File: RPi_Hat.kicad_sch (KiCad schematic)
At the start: 34 parts, among them IC1 0.96_I2C_OLED, IC2 0.96_I2C_OLED, J1 RPi_GPIO, J2 TCBM, J3 Conn_01x05, J4 Mini-DIN-7, Q1 NPN: 2n3904, Q2 NPN: 2n3904, Q3 NPN: 2n3904, Q4 NPN: 2n3904, SW1 Select, SW2 Up, SW3 Down, SW4 Exit, SW5 Add Disk

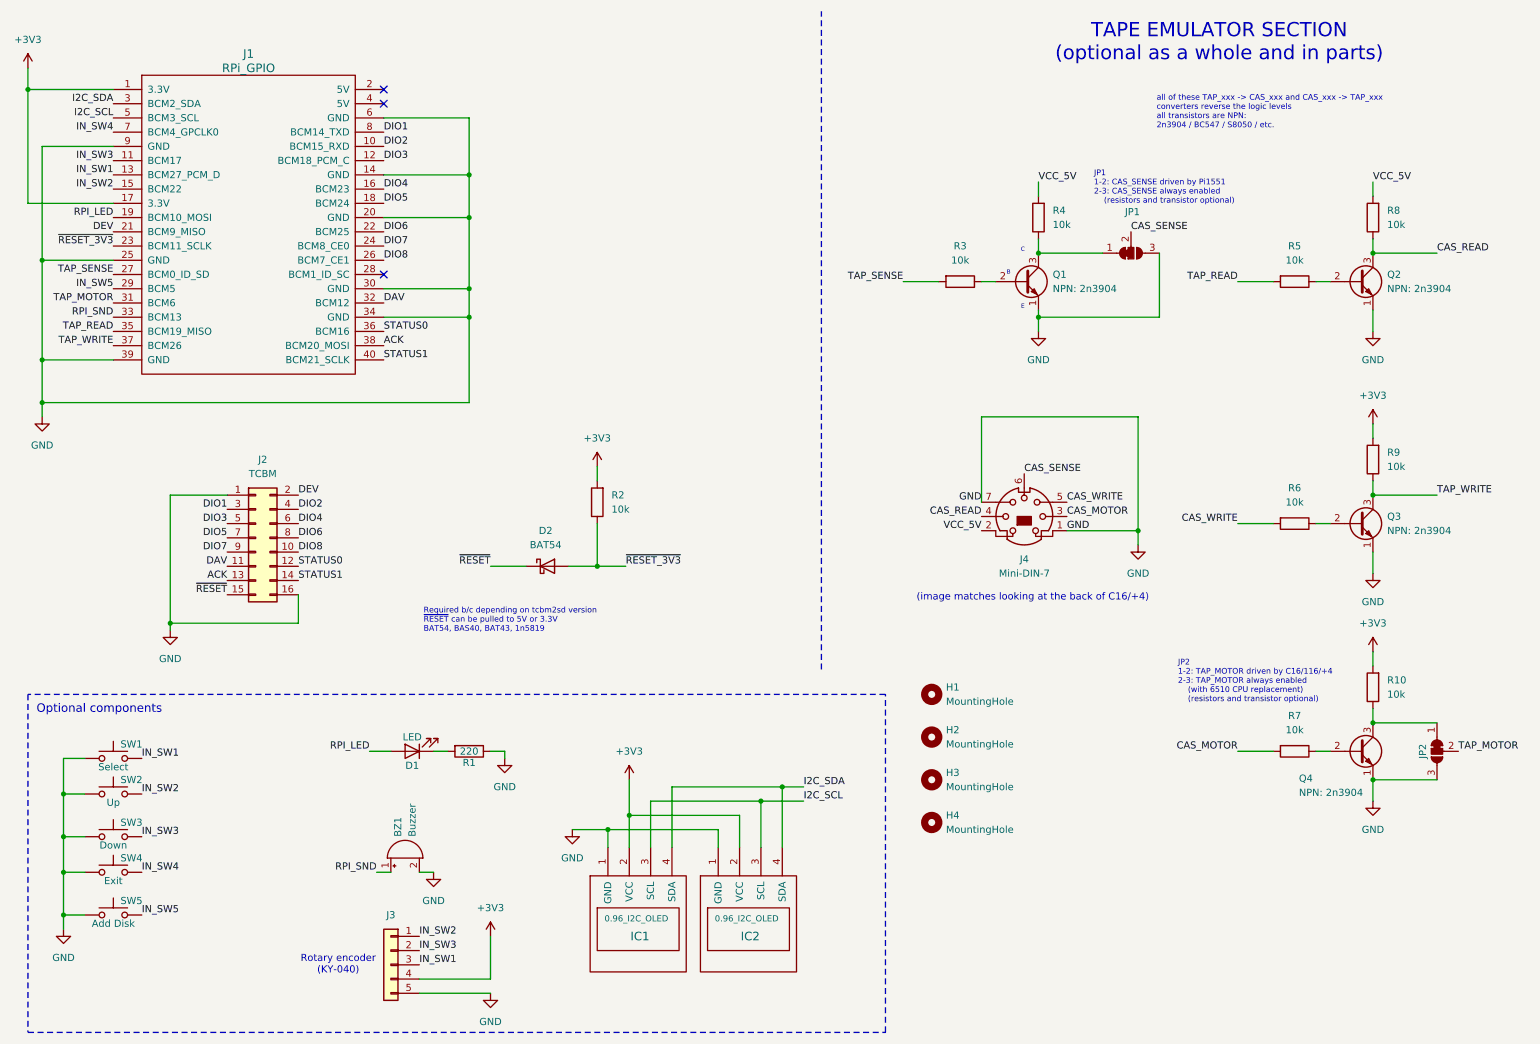
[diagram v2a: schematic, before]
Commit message: SMD rework and updates
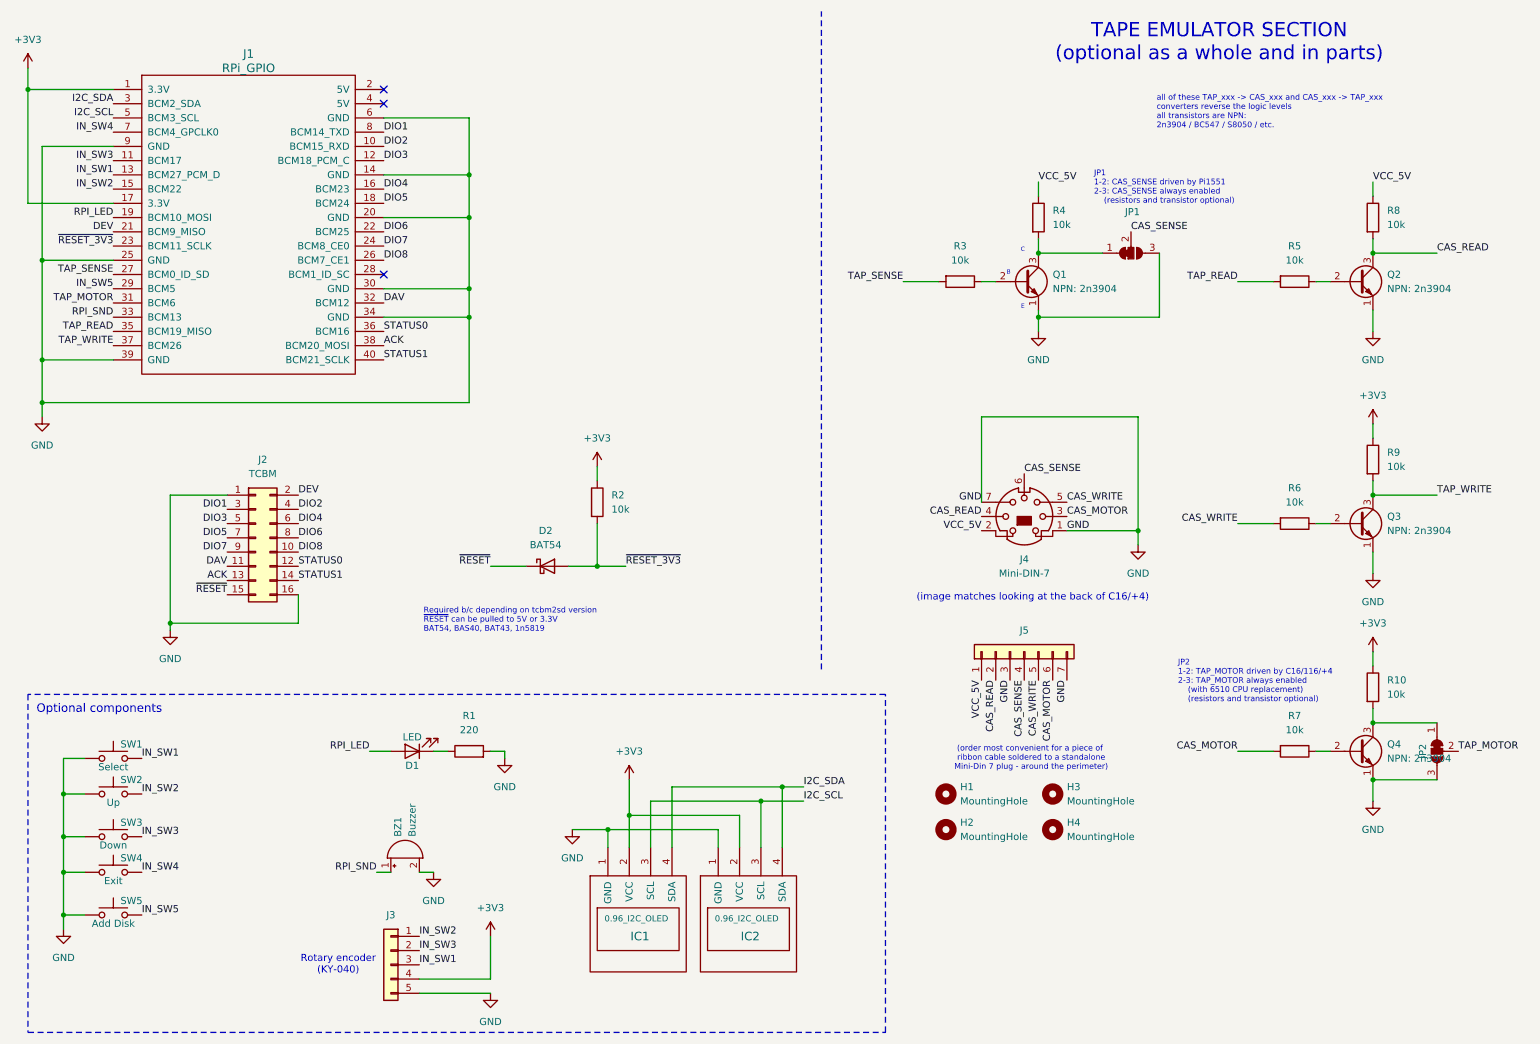
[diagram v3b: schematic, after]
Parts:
- added J5: Conn_01x07, Connector_PinHeader_2.54mm:PinHeader_1x07_P2.54mm_Horizontal, symbol Connector_Generic:Conn_01x07
- D1: footprint LED_THT:LED_D5.0mm -> LED_THT:LED_D3.0mm
- D2: footprint Diode_THT:D_A-405_P7.62mm_Horizontal -> Diode_SMD:D_SOD-123; JLCPCB Part # (none) -> C7502705; JLCPCB URL (none) -> https://jlcpcb.com/partdetail/hongjiacheng-BAT54W/C7502705; MFR.Part # (none) -> BAT54W
- J4: footprint Connector_PinHeader_2.54mm:PinHeader_1x07_P2.54mm_Vertical -> Conn_DIN_round:Mini_DIN_round_7_canned
- Q1, Q2, Q3, Q4: footprint Package_TO_SOT_THT:TO-92_Inline -> Package_TO_SOT_SMD:SOT-23_Handsoldering; JLCPCB Part # (none) -> C18536; JLCPCB URL (none) -> https://jlcpcb.com/partdetail/KECSemicon-2N3904S_RTKPS/C185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; MFR.Part # (none) -> 2N3904S-RTK/PS
- R1: footprint Resistor_THT:R_Axial_DIN0207_L6.3mm_D2.5mm_P10.16mm_Horizontal -> Resistor_SMD:R_0805_2012Metric_Pad1.20x1.40mm_HandSolder; JLCPCB Part # (none) -> C17557; JLCPCB URL (none) -> https://jlcpcb.com/partdetail/18245-0805W8F2200T5E/C17557; MFR.Part # (none) -> 0805W8F2200T5E
- R10, R2, R3, R4, R5, R6, R7, R8, R9: footprint Resistor_THT:R_Axial_DIN0207_L6.3mm_D2.5mm_P10.16mm_Horizontal -> Resistor_SMD:R_0805_2012Metric_Pad1.20x1.40mm_HandSolder; JLCPCB Part # (none) -> C22356686; JLCPCB URL (none) -> https://jlcpcb.com/partdetail/23790130-RCA0510KFLF/C22356686; MFR.Part # (none) -> RCA0510KFLF
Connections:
- net +3V3: now also R10.1, R2.1, R9.1; no longer R10.2, R2.2, R9.2
- net CAS_MOTOR: now also J5.6 (Pin_6)
- net CAS_READ: now also R8.2, J5.2 (Pin_2); no longer R8.1
- net CAS_SENSE: now also J5.4 (Pin_4)
- net CAS_WRITE: now also J5.5 (Pin_5)
- net GND: now also R1.2, J5.3 (Pin_3), J5.7 (Pin_7); no longer R1.1
- net TAP_WRITE: now also R9.2; no longer R9.1
- net VCC_5V: now also R4.1, R8.1, J5.1 (Pin_1); no longer R4.2, R8.2
- net ~{RESET_3V3}: now also R2.2; no longer R2.1
- net at D1.1 (K): now also R1.1; no longer R1.2
- net at JP1.1 (A), Q1.3 (C): now also R4.2; no longer R4.1
- net at JP2.1 (A), Q4.3 (C): now also R10.2; no longer R10.1
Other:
- note added: "(order most convenient for a piece of ribbon cable soldered to a standalone Mini-Din 7 plug - around the perimeter)"
- moved on the sheet: H1, H2, H3, H4

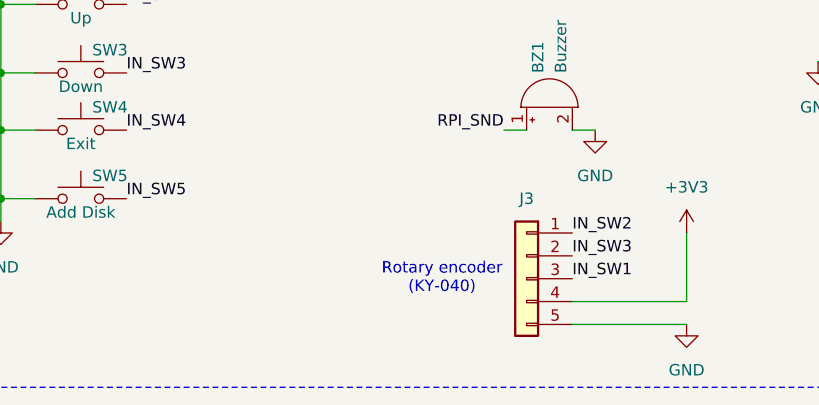
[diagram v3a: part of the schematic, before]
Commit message: final version for test fabrication, added encoder part directly (without module, without pullups)
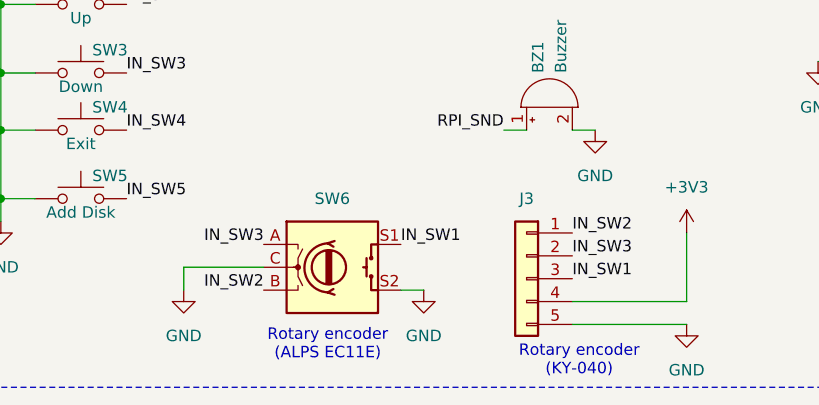
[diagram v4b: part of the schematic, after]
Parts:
- added SW6: RotaryEncoder_Switch, Rotary_Encoder:RotaryEncoder_Alps_EC11E-Switch_Vertical_H20mm_CircularMountingHoles, symbol Device:RotaryEncoder_Switch
- BZ1, D1, IC1, IC2, J1, J2, J3, J4, J5, SW1, SW2, SW3, SW4, SW5: now left out of the parts list
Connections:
- net GND: now also SW6.C, SW6.S2
- net IN_SW1: now also SW6.S1
- net IN_SW2: now also SW6.B
- net IN_SW3: now also SW6.A
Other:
- note added: "Rotary encoder (ALPS EC11E)"

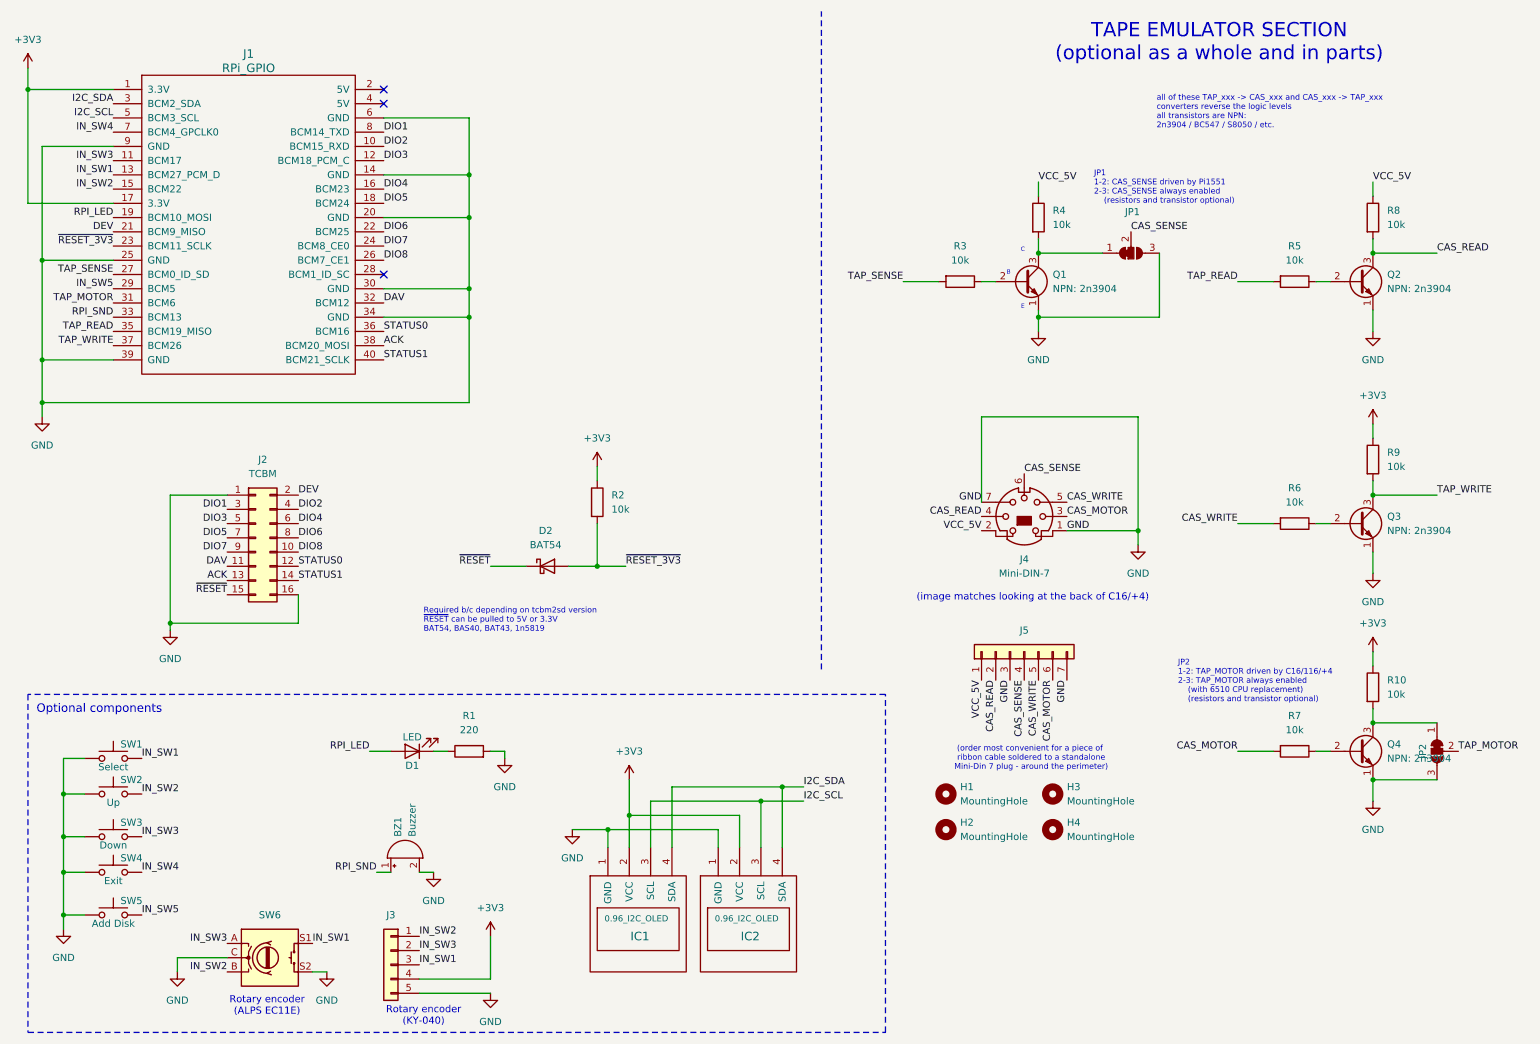
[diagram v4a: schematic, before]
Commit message: - correct part and pinout for SMD 2n3904 transistor - added jumpers to configure VCC/GND routing for OLED screens - moved encoder to the left, module socket to the right
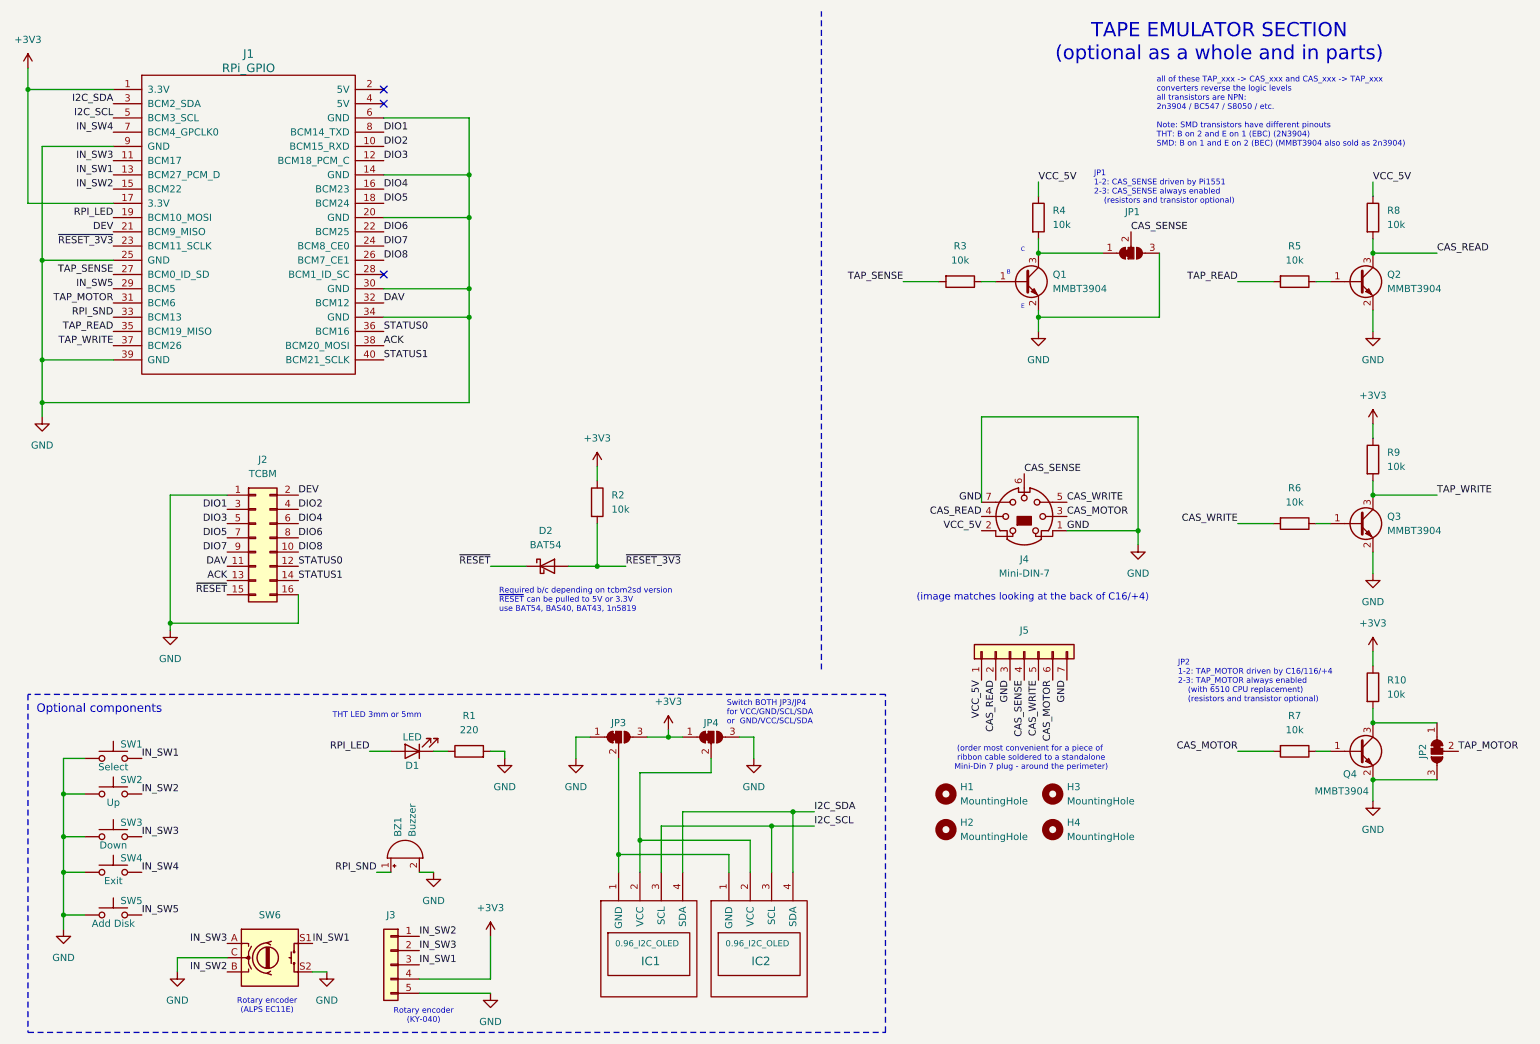
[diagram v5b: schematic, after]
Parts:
- removed Q1, Q2, Q3, Q4: NPN: 2n3904, Package_TO_SOT_SMD:SOT-23_Handsoldering, symbol Transistor_BJT:2N3904
- added JP3, JP4: SolderJumper_3_Bridged12, Jumper:SolderJumper-3_P1.3mm_Bridged12_RoundedPad1.0x1.5mm_NumberLabels, symbol Jumper:SolderJumper_3_Bridged12
- added Q1, Q2, Q3, Q4: MMBT3904, Package_TO_SOT_SMD:SOT-23_Handsoldering, symbol Transistor_BJT:MMBT3904
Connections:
- net +3V3: now also JP3.3 (B), JP4.1 (A); no longer IC1.2 (VCC), IC2.2 (VCC)
- net CAS_READ: now also Q2.3 (C)
- net GND: now also JP3.1 (A), JP4.3 (B), Q1.2 (E), Q2.2 (E), Q3.2 (E), Q4.2 (E); no longer IC1.1 (GND), IC2.1 (GND)
- net TAP_WRITE: now also Q3.3 (C)
- net at R7.1: now also Q4.1 (B)
- net at R5.1: now also Q2.1 (B)
- net at JP1.1 (A), R4.2: now also Q1.3 (C)
- net at JP2.1 (A), R10.2: now also Q4.3 (C)
- net at R6.1: now also Q3.1 (B)
- net at R3.1: now also Q1.1 (B)
- new net: IC1.1 (GND), IC2.1 (GND), JP3.2 (C)
- new net: IC1.2 (VCC), IC2.2 (VCC), JP4.2 (C)
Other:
- note added: "Required b/c depending on tcbm2sd version ~{RESET} can be pulled to 5V or 3.3V use BAT54, BAS40, BAT43, 1n5819"
- note added: "Switch BOTH JP3/JP4 for VCC/GND/SCL/SDA or GND/VCC/SCL/SDA"
- note added: "THT LED 3mm or 5mm"
- note added: "all of these TAP_xxx -> CAS_xxx and CAS_xxx -> TAP_xxx converters reverse the logic levels all transistors are NPN: 2n3904 / BC547 / S8050 / etc. Note: SMD transistors have different pinouts THT: B on 2 and E on 1 (EBC) (2N3904) SMD: B on 1 and E on 2 (BEC) (MMBT3904 also sold as 2n3904)"
- note removed: "Required b/c depending on tcbm2sd version ~{RESET} can be pulled to 5V or 3.3V BAT54, BAS40, BAT43, 1n5819"
- note removed: "all of these TAP_xxx -> CAS_xxx and CAS_xxx -> TAP_xxx converters reverse the logic levels all transistors are NPN: 2n3904 / BC547 / S8050 / etc."
- moved on the sheet: IC1, IC2
